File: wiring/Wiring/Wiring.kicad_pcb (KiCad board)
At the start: 2 copper layers, 4 parts, among them U1 MAIN, U2 E, U3 F, U4 G

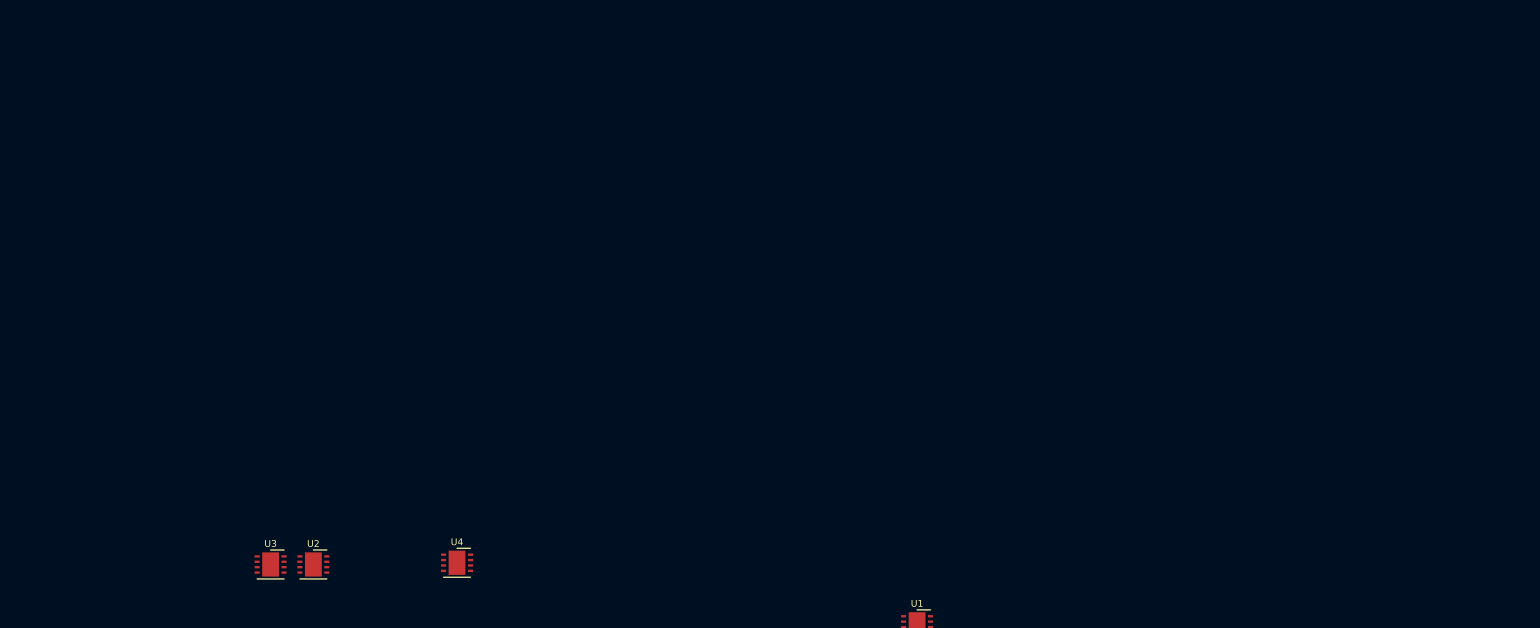
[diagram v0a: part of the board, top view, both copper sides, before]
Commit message: Add more boxes
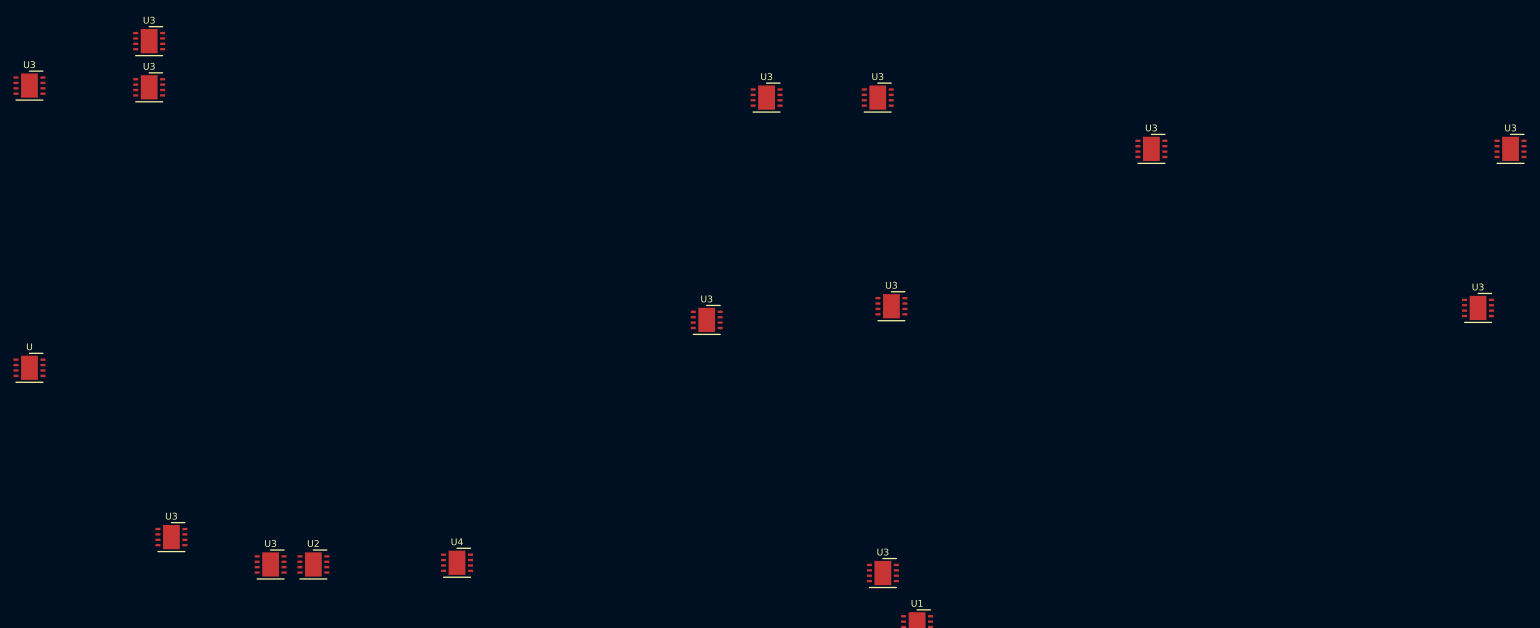
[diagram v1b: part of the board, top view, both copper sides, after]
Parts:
- added U: L, Package_DFN_QFN:DFN-8-1EP_4x4mm_P0.8mm_EP2.5x3.6mm, F.Cu at (18.8, 96.0)
- added U3: F, Package_DFN_QFN:DFN-8-1EP_4x4mm_P0.8mm_EP2.5x3.6mm, F.Cu at (119.4, 88.9)
- added U3: C, Package_DFN_QFN:DFN-8-1EP_4x4mm_P0.8mm_EP2.5x3.6mm, F.Cu at (36.6, 47.5)
- added U3: A, Package_DFN_QFN:DFN-8-1EP_4x4mm_P0.8mm_EP2.5x3.6mm, F.Cu at (18.8, 54.1)
- added U3: D, Package_DFN_QFN:DFN-8-1EP_4x4mm_P0.8mm_EP2.5x3.6mm, F.Cu at (39.9, 121.2)
- added U3: O, Package_DFN_QFN:DFN-8-1EP_4x4mm_P0.8mm_EP2.5x3.6mm, F.Cu at (144.8, 55.9)
- added U3: N, Package_DFN_QFN:DFN-8-1EP_4x4mm_P0.8mm_EP2.5x3.6mm, F.Cu at (238.8, 63.5)
- added U3: M, Package_DFN_QFN:DFN-8-1EP_4x4mm_P0.8mm_EP2.5x3.6mm, F.Cu at (233.9, 87.1)
- added U3: H, Package_DFN_QFN:DFN-8-1EP_4x4mm_P0.8mm_EP2.5x3.6mm, F.Cu at (146.8, 86.9)
- added U3: J, Package_DFN_QFN:DFN-8-1EP_4x4mm_P0.8mm_EP2.5x3.6mm, F.Cu at (185.4, 63.5)
- added U3: I, Package_DFN_QFN:DFN-8-1EP_4x4mm_P0.8mm_EP2.5x3.6mm, F.Cu at (145.5, 126.5)
- added U3: K, Package_DFN_QFN:DFN-8-1EP_4x4mm_P0.8mm_EP2.5x3.6mm, F.Cu at (128.3, 55.9)
- added U3: B, Package_DFN_QFN:DFN-8-1EP_4x4mm_P0.8mm_EP2.5x3.6mm, F.Cu at (36.6, 54.4)

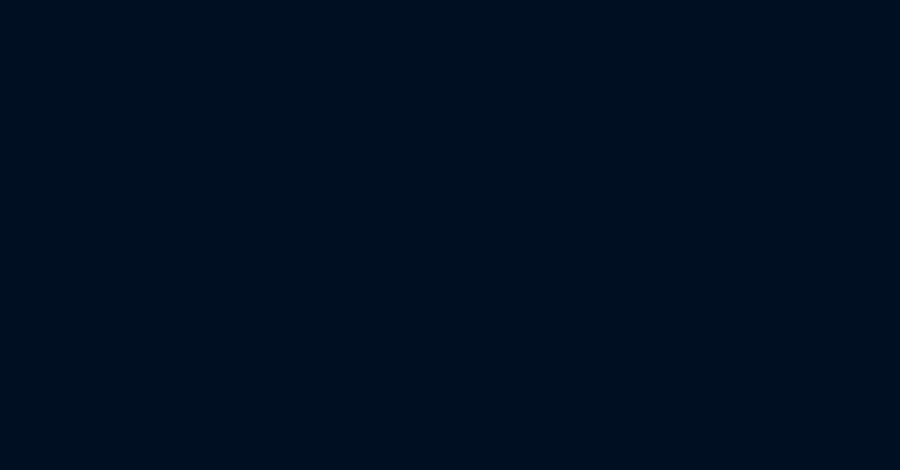
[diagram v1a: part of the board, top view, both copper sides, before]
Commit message: Add one more box
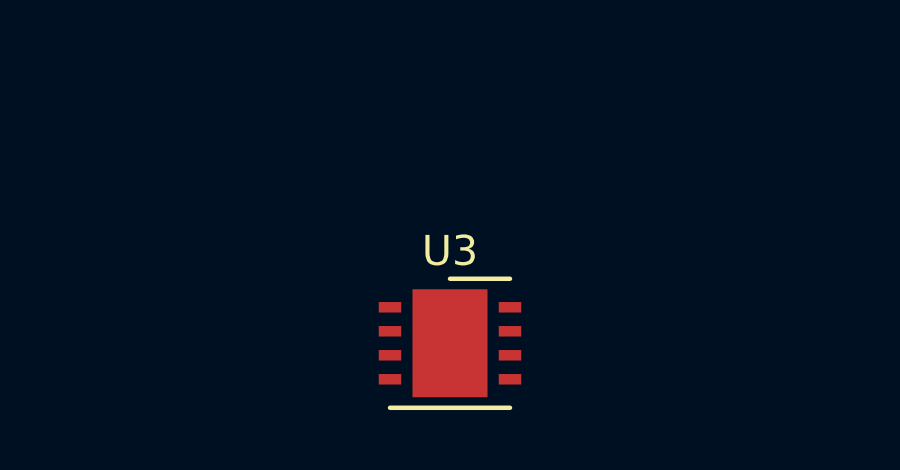
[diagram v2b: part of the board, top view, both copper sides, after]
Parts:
- added U3: Q, Package_DFN_QFN:DFN-8-1EP_4x4mm_P0.8mm_EP2.5x3.6mm, F.Cu at (38.4, 145.5)
- U3: value F -> P
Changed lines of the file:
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@@
     (tracks 0)
     (zones 0)
-    (modules 17)
+    (modules 18)
     (nets 27)
   )
@@
   )
   (module Package_DFN_QFN:DFN-8-1EP_4x4mm_P0.8mm_EP2.5x3.6mm (layer F.Cu)
+    (at 38.354 145.542)
+    (descr "8-Lead Plastic Dual Flat, No Lead Package (MD) - 4x4x0.9 mm Body [DFN] (see Microchip Packaging Specification 00000049BS.pdf)")
+    (tags "DFN 0.8")
+    (attr smd)
+    (fp_text reference U3 (at 0 -3.075) (layer F.SilkS)
+      (effects (font (size 1 1) (thickness 0.15)))
+    )
+    (fp_text value Q (at 0 3.075) (layer F.Fab)
+      (effects (font (size 1 1) (thickness 0.15)))
+    )
+    (fp_line (start 0 -2.15) (end 2 -2.15) (layer F.SilkS) (width 0.15))
+    (fp_line (start -2 2.15) (end 2 2.15) (layer F.SilkS) (width 0.15))
+    (fp_line (start -2.65 2.35) (end 2.65 2.35) (layer F.CrtYd) (width 0.05))
+    (fp_line (start -2.65 -2.35) (end 2.65 -2.35) (layer F.CrtYd) (width 0.05))
+    (fp_line (start 2.65 -2.35) (end 2.65 2.35) (layer F.CrtYd) (width 0.05))
+    (fp_line (start -2.65 -2.35) (end -2.65 2.35) (layer F.CrtYd) (width 0.05))
+    (fp_line (start -2 -1) (end -1 -2) (layer F.Fab) (width 0.15))
+    (fp_line (start -2 2) (end -2 -1) (layer F.Fab) (width 0.15))
+    (fp_line (start 2 2) (end -2 2) (layer F.Fab) (width 0.15))
+    (fp_line (start 2 -2) (end 2 2) (layer F.Fab) (width 0.15))
+    (fp_line (start -1 -2) (end 2 -2) (layer F.Fab) (width 0.15))
+    (fp_text user %R (at 0 0) (layer F.Fab)
+      (effects (font (size 1 1) (thickness 0.15)))
+    )
+    (pad "" smd rect (at -0.625 1.2) (size 1 1) (layers F.Paste))
+    (pad "" smd rect (at 0.625 1.2) (size 1 1) (layers F.Paste))
+    (pad "" smd rect (at -0.625 0) (size 1 1) (layers F.Paste))
+    (pad "" smd rect (at 0.625 0) (size 1 1) (layers F.Paste))
+    (pad "" smd rect (at 0.625 -1.2) (size 1 1) (layers F.Paste))
+    (pad 9 smd rect (at 0 0) (size 2.5 3.6) (layers F.Cu F.Mask))
+    (pad "" smd rect (at -0.625 -1.2) (size 1 1) (layers F.Paste))
+    (pad 8 smd rect (at 2 -1.2) (size 0.75 0.35) (layers F.Cu F.Paste F.Mask))
+    (pad 7 smd rect (at 2 -0.4) (size 0.75 0.35) (layers F.Cu F.Paste F.Mask))
+    (pad 6 smd rect (at 2 0.4) (size 0.75 0.35) (layers F.Cu F.Paste F.Mask))
+    (pad 5 smd rect (at 2 1.2) (size 0.75 0.35) (layers F.Cu F.Paste F.Mask))
+    (pad 4 smd rect (at -2 1.2) (size 0.75 0.35) (layers F.Cu F.Paste F.Mask))
+    (pad 3 smd rect (at -2 0.4) (size 0.75 0.35) (layers F.Cu F.Paste F.Mask))
+    (pad 2 smd rect (at -2 -0.4) (size 0.75 0.35) (layers F.Cu F.Paste F.Mask))
+    (pad 1 smd rect (at -2 -1.2) (size 0.75 0.35) (layers F.Cu F.Paste F.Mask))
+    (model ${KISYS3DMOD}/Package_DFN_QFN.3dshapes/DFN-8-1EP_4x4mm_P0.8mm_EP2.5x3.6mm.wrl
+      (at (xyz 0 0 0))
+      (scale (xyz 1 1 1))
+      (rotate (xyz 0 0 0))
+    )
+  )
+  (module Package_DFN_QFN:DFN-8-1EP_4x4mm_P0.8mm_EP2.5x3.6mm (layer F.Cu)
     (at 119.38 88.9)
     (descr "8-Lead Plastic Dual Flat, No Lead Package (MD) - 4x4x0.9 mm Body [DFN] (see Microchip Packaging Specification 00000049BS.pdf)")
@@
       (effects (font (size 1 1) (thickness 0.15)))
     )
-    (fp_text value F (at 0 3.075) (layer F.Fab)
-      (effects (font (size 1 1) (thickness 0.15)))
-    )
+    (fp_text value P (at 0 3.075) (layer F.Fab)
+      (effects (font (size 1 1) (thickness 0.15)))
+    )

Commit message: Add yet more boxes
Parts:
- added U3: T, Package_DFN_QFN:DFN-8-1EP_4x4mm_P0.8mm_EP2.5x3.6mm, F.Cu at (137.9, 121.4)
- added U3: R, Package_DFN_QFN:DFN-8-1EP_4x4mm_P0.8mm_EP2.5x3.6mm, F.Cu at (241.6, 87.1)
- added U3: S, Package_DFN_QFN:DFN-8-1EP_4x4mm_P0.8mm_EP2.5x3.6mm, F.Cu at (277.1, 94.7)
- moved U1 6.88 mm to (157.5, 134.6)
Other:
- board text added: "DOOR"
- board text added: "LOO"
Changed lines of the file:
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@@
   (general
     (thickness 1.6)
-    (drawings 44)
+    (drawings 50)
     (tracks 0)
     (zones 0)
-    (modules 18)
+    (modules 21)
     (nets 27)
   )
@@
     (pad_to_mask_clearance 0.05)
     (aux_axis_origin 0 0)
-    (visible_elements FFE2B027)
+    (visible_elements FFE2A027)
     (pcbplotparams
       (layerselection 0x010fc_ffffffff)
@@
   )
   (module Package_DFN_QFN:DFN-8-1EP_4x4mm_P0.8mm_EP2.5x3.6mm (layer F.Cu)
+    (at 137.922 121.412)
+    (descr "8-Lead Plastic Dual Flat, No Lead Package (MD) - 4x4x0.9 mm Body [DFN] (see Microchip Packaging Specification 00000049BS.pdf)")
+    (tags "DFN 0.8")
+    (attr smd)
+    (fp_text reference U3 (at 0 -3.075) (layer F.SilkS)
+      (effects (font (size 1 1) (thickness 0.15)))
+    )
+    (fp_text value T (at 0 3.075) (layer F.Fab)
+      (effects (font (size 1 1) (thickness 0.15)))
+    )
+    (fp_line (start 0 -2.15) (end 2 -2.15) (layer F.SilkS) (width 0.15))
+    (fp_line (start -2 2.15) (end 2 2.15) (layer F.SilkS) (width 0.15))
+    (fp_line (start -2.65 2.35) (end 2.65 2.35) (layer F.CrtYd) (width 0.05))
+    (fp_line (start -2.65 -2.35) (end 2.65 -2.35) (layer F.CrtYd) (width 0.05))
+    (fp_line (start 2.65 -2.35) (end 2.65 2.35) (layer F.CrtYd) (width 0.05))
+    (fp_line (start -2.65 -2.35) (end -2.65 2.35) (layer F.CrtYd) (width 0.05))
+    (fp_line (start -2 -1) (end -1 -2) (layer F.Fab) (width 0.15))
+    (fp_line (start -2 2) (end -2 -1) (layer F.Fab) (width 0.15))
+    (fp_line (start 2 2) (end -2 2) (layer F.Fab) (width 0.15))
+    (fp_line (start 2 -2) (end 2 2) (layer F.Fab) (width 0.15))
+    (fp_line (start -1 -2) (end 2 -2) (layer F.Fab) (width 0.15))
+    (fp_text user %R (at 0 0) (layer F.Fab)
+      (effects (font (size 1 1) (thickness 0.15)))
+    )
+    (pad 1 smd rect (at -2 -1.2) (size 0.75 0.35) (layers F.Cu F.Paste F.Mask))
+    (pad 2 smd rect (at -2 -0.4) (size 0.75 0.35) (layers F.Cu F.Paste F.Mask))
+    (pad 3 smd rect (at -2 0.4) (size 0.75 0.35) (layers F.Cu F.Paste F.Mask))
+    (pad 4 smd rect (at -2 1.2) (size 0.75 0.35) (layers F.Cu F.Paste F.Mask))
+    (pad 5 smd rect (at 2 1.2) (size 0.75 0.35) (layers F.Cu F.Paste F.Mask))
+    (pad 6 smd rect (at 2 0.4) (size 0.75 0.35) (layers F.Cu F.Paste F.Mask))
+    (pad 7 smd rect (at 2 -0.4) (size 0.75 0.35) (layers F.Cu F.Paste F.Mask))
+    (pad 8 smd rect (at 2 -1.2) (size 0.75 0.35) (layers F.Cu F.Paste F.Mask))
+    (pad "" smd rect (at -0.625 -1.2) (size 1 1) (layers F.Paste))
+    (pad 9 smd rect (at 0 0) (size 2.5 3.6) (layers F.Cu F.Mask))
+    (pad "" smd rect (at 0.625 -1.2) (size 1 1) (layers F.Paste))
+    (pad "" smd rect (at 0.625 0) (size 1 1) (layers F.Paste))
+    (pad "" smd rect (at -0.625 0) (size 1 1) (layers F.Paste))
+    (pad "" smd rect (at 0.625 1.2) (size 1 1) (layers F.Paste))
+    (pad "" smd rect (at -0.625 1.2) (size 1 1) (layers F.Paste))
+    (model ${KISYS3DMOD}/Package_DFN_QFN.3dshapes/DFN-8-1EP_4x4mm_P0.8mm_EP2.5x3.6mm.wrl
+      (at (xyz 0 0 0))
+      (scale (xyz 1 1 1))
+      (rotate (xyz 0 0 0))
+    )
+  )
+  (module Package_DFN_QFN:DFN-8-1EP_4x4mm_P0.8mm_EP2.5x3.6mm (layer F.Cu)
+    (at 241.554 87.122)
+    (descr "8-Lead Plastic Dual Flat, No Lead Package (MD) - 4x4x0.9 mm Body [DFN] (see Microchip Packaging Specification 00000049BS.pdf)")
+    (tags "DFN 0.8")
+    (attr smd)
+    (fp_text reference U3 (at 0 -3.075) (layer F.SilkS)
+      (effects (font (size 1 1) (thickness 0.15)))
+    )
+    (fp_text value R (at 0 3.075) (layer F.Fab)
+      (effects (font (size 1 1) (thickness 0.15)))
+    )
+    (fp_line (start 0 -2.15) (end 2 -2.15) (layer F.SilkS) (width 0.15))
+    (fp_line (start -2 2.15) (end 2 2.15) (layer F.SilkS) (width 0.15))
+    (fp_line (start -2.65 2.35) (end 2.65 2.35) (layer F.CrtYd) (width 0.05))
+    (fp_line (start -2.65 -2.35) (end 2.65 -2.35) (layer F.CrtYd) (width 0.05))
+    (fp_line (start 2.65 -2.35) (end 2.65 2.35) (layer F.CrtYd) (width 0.05))
+    (fp_line (start -2.65 -2.35) (end -2.65 2.35) (layer F.CrtYd) (width 0.05))
+    (fp_line (start -2 -1) (end -1 -2) (layer F.Fab) (width 0.15))
+    (fp_line (start -2 2) (end -2 -1) (layer F.Fab) (width 0.15))
+    (fp_line (start 2 2) (end -2 2) (layer F.Fab) (width 0.15))
+    (fp_line (start 2 -2) (end 2 2) (layer F.Fab) (width 0.15))
+    (fp_line (start -1 -2) (end 2 -2) (layer F.Fab) (width 0.15))
+    (fp_text user %R (at 0 0) (layer F.Fab)
+      (effects (font (size 1 1) (thickness 0.15)))
+    )
+    (pad 1 smd rect (at -2 -1.2) (size 0.75 0.35) (layers F.Cu F.Paste F.Mask))
+    (pad 2 smd rect (at -2 -0.4) (size 0.75 0.35) (layers F.Cu F.Paste F.Mask))
+    (pad 3 smd rect (at -2 0.4) (size 0.75 0.35) (layers F.Cu F.Paste F.Mask))
+    (pad 4 smd rect (at -2 1.2) (size 0.75 0.35) (layers F.Cu F.Paste F.Mask))
+    (pad 5 smd rect (at 2 1.2) (size 0.75 0.35) (layers F.Cu F.Paste F.Mask))
+    (pad 6 smd rect (at 2 0.4) (size 0.75 0.35) (layers F.Cu F.Paste F.Mask))
+    (pad 7 smd rect (at 2 -0.4) (size 0.75 0.35) (layers F.Cu F.Paste F.Mask))
+    (pad 8 smd rect (at 2 -1.2) (size 0.75 0.35) (layers F.Cu F.Paste F.Mask))
+    (pad "" smd rect (at -0.625 -1.2) (size 1 1) (layers F.Paste))
+    (pad 9 smd rect (at 0 0) (size 2.5 3.6) (layers F.Cu F.Mask))
+    (pad "" smd rect (at 0.625 -1.2) (size 1 1) (layers F.Paste))
+    (pad "" smd rect (at 0.625 0) (size 1 1) (layers F.Paste))
+    (pad "" smd rect (at -0.625 0) (size 1 1) (layers F.Paste))
+    (pad "" smd rect (at 0.625 1.2) (size 1 1) (layers F.Paste))
+    (pad "" smd rect (at -0.625 1.2) (size 1 1) (layers F.Paste))
+    (model ${KISYS3DMOD}/Package_DFN_QFN.3dshapes/DFN-8-1EP_4x4mm_P0.8mm_EP2.5x3.6mm.wrl
+      (at (xyz 0 0 0))
+      (scale (xyz 1 1 1))
+      (rotate (xyz 0 0 0))
+    )
+  )
+  (module Package_DFN_QFN:DFN-8-1EP_4x4mm_P0.8mm_EP2.5x3.6mm (layer F.Cu)
+    (at 277.114 94.742)
+    (descr "8-Lead Plastic Dual Flat, No Lead Package (MD) - 4x4x0.9 mm Body [DFN] (see Microchip Packaging Specification 00000049BS.pdf)")
+    (tags "DFN 0.8")
+    (attr smd)
+    (fp_text reference U3 (at 0 -3.075) (layer F.SilkS)
+      (effects (font (size 1 1) (thickness 0.15)))
+    )
+    (fp_text value S (at 0 3.075) (layer F.Fab)
+      (effects (font (size 1 1) (thickness 0.15)))
+    )
+    (fp_line (start 0 -2.15) (end 2 -2.15) (layer F.SilkS) (width 0.15))
+    (fp_line (start -2 2.15) (end 2 2.15) (layer F.SilkS) (width 0.15))
+    (fp_line (start -2.65 2.35) (end 2.65 2.35) (layer F.CrtYd) (width 0.05))
+    (fp_line (start -2.65 -2.35) (end 2.65 -2.35) (layer F.CrtYd) (width 0.05))
+    (fp_line (start 2.65 -2.35) (end 2.65 2.35) (layer F.CrtYd) (width 0.05))
+    (fp_line (start -2.65 -2.35) (end -2.65 2.35) (layer F.CrtYd) (width 0.05))
+    (fp_line (start -2 -1) (end -1 -2) (layer F.Fab) (width 0.15))
+    (fp_line (start -2 2) (end -2 -1) (layer F.Fab) (width 0.15))
+    (fp_line (start 2 2) (end -2 2) (layer F.Fab) (width 0.15))
+    (fp_line (start 2 -2) (end 2 2) (layer F.Fab) (width 0.15))
+    (fp_line (start -1 -2) (end 2 -2) (layer F.Fab) (width 0.15))
+    (fp_text user %R (at 0 0) (layer F.Fab)
+      (effects (font (size 1 1) (thickness 0.15)))
+    )
+    (pad 1 smd rect (at -2 -1.2) (size 0.75 0.35) (layers F.Cu F.Paste F.Mask))
+    (pad 2 smd rect (at -2 -0.4) (size 0.75 0.35) (layers F.Cu F.Paste F.Mask))
+    (pad 3 smd rect (at -2 0.4) (size 0.75 0.35) (layers F.Cu F.Paste F.Mask))
+    (pad 4 smd rect (at -2 1.2) (size 0.75 0.35) (layers F.Cu F.Paste F.Mask))
+    (pad 5 smd rect (at 2 1.2) (size 0.75 0.35) (layers F.Cu F.Paste F.Mask))
+    (pad 6 smd rect (at 2 0.4) (size 0.75 0.35) (layers F.Cu F.Paste F.Mask))
+    (pad 7 smd rect (at 2 -0.4) (size 0.75 0.35) (layers F.Cu F.Paste F.Mask))
+    (pad 8 smd rect (at 2 -1.2) (size 0.75 0.35) (layers F.Cu F.Paste F.Mask))
+    (pad "" smd rect (at -0.625 -1.2) (size 1 1) (layers F.Paste))
+    (pad 9 smd rect (at 0 0) (size 2.5 3.6) (layers F.Cu F.Mask))
+    (pad "" smd rect (at 0.625 -1.2) (size 1 1) (layers F.Paste))
+    (pad "" smd rect (at 0.625 0) (size 1 1) (layers F.Paste))
+    (pad "" smd rect (at -0.625 0) (size 1 1) (layers F.Paste))
+    (pad "" smd rect (at 0.625 1.2) (size 1 1) (layers F.Paste))
+    (pad "" smd rect (at -0.625 1.2) (size 1 1) (layers F.Paste))
+    (model ${KISYS3DMOD}/Package_DFN_QFN.3dshapes/DFN-8-1EP_4x4mm_P0.8mm_EP2.5x3.6mm.wrl
+      (at (xyz 0 0 0))
+      (scale (xyz 1 1 1))
+      (rotate (xyz 0 0 0))
+    )
+  )
+  (module Package_DFN_QFN:DFN-8-1EP_4x4mm_P0.8mm_EP2.5x3.6mm (layer F.Cu)
     (at 38.354 145.542)
     (descr "8-Lead Plastic Dual Flat, No Lead Package (MD) - 4x4x0.9 mm Body [DFN] (see Microchip Packaging Specification 00000049BS.pdf)")
@@
   )
   (module Package_DFN_QFN:DFN-8-1EP_4x4mm_P0.8mm_EP2.5x3.6mm (layer F.Cu)
-    (at 150.622 134.112)
+    (at 157.48 134.62)
     (descr "8-Lead Plastic Dual Flat, No Lead Package (MD) - 4x4x0.9 mm Body [DFN] (see Microchip Packaging Specification 00000049BS.pdf)")
     (tags "DFN 0.8")
@@
     )
   )
+  (gr_line (start 149.86 137.16) (end 149.86 132.08) (layer Cmts.User) (width 0.15))
+  (gr_line (start 162.56 137.16) (end 149.86 137.16) (layer Cmts.User) (width 0.15))
+  (gr_line (start 162.56 132.08) (end 162.56 137.16) (layer Cmts.User) (width 0.15))
+  (gr_line (start 149.86 132.08) (end 162.56 132.08) (layer Cmts.User) (width 0.15))
+  (gr_text LOO (at 261.62 91.44) (layer Cmts.User)
+    (effects (font (size 1 1) (thickness 0.15)))
+  )
+  (gr_text DOOR (at 71.12 132.08) (layer Cmts.User)
+    (effects (font (size 1 1) (thickness 0.15)))
+  )
   (gr_line (start 121.92 104.14) (end 116.84 104.14) (layer Cmts.User) (width 0.15))
